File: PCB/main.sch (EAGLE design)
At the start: 55 parts, among them X1 BU-SMA-V

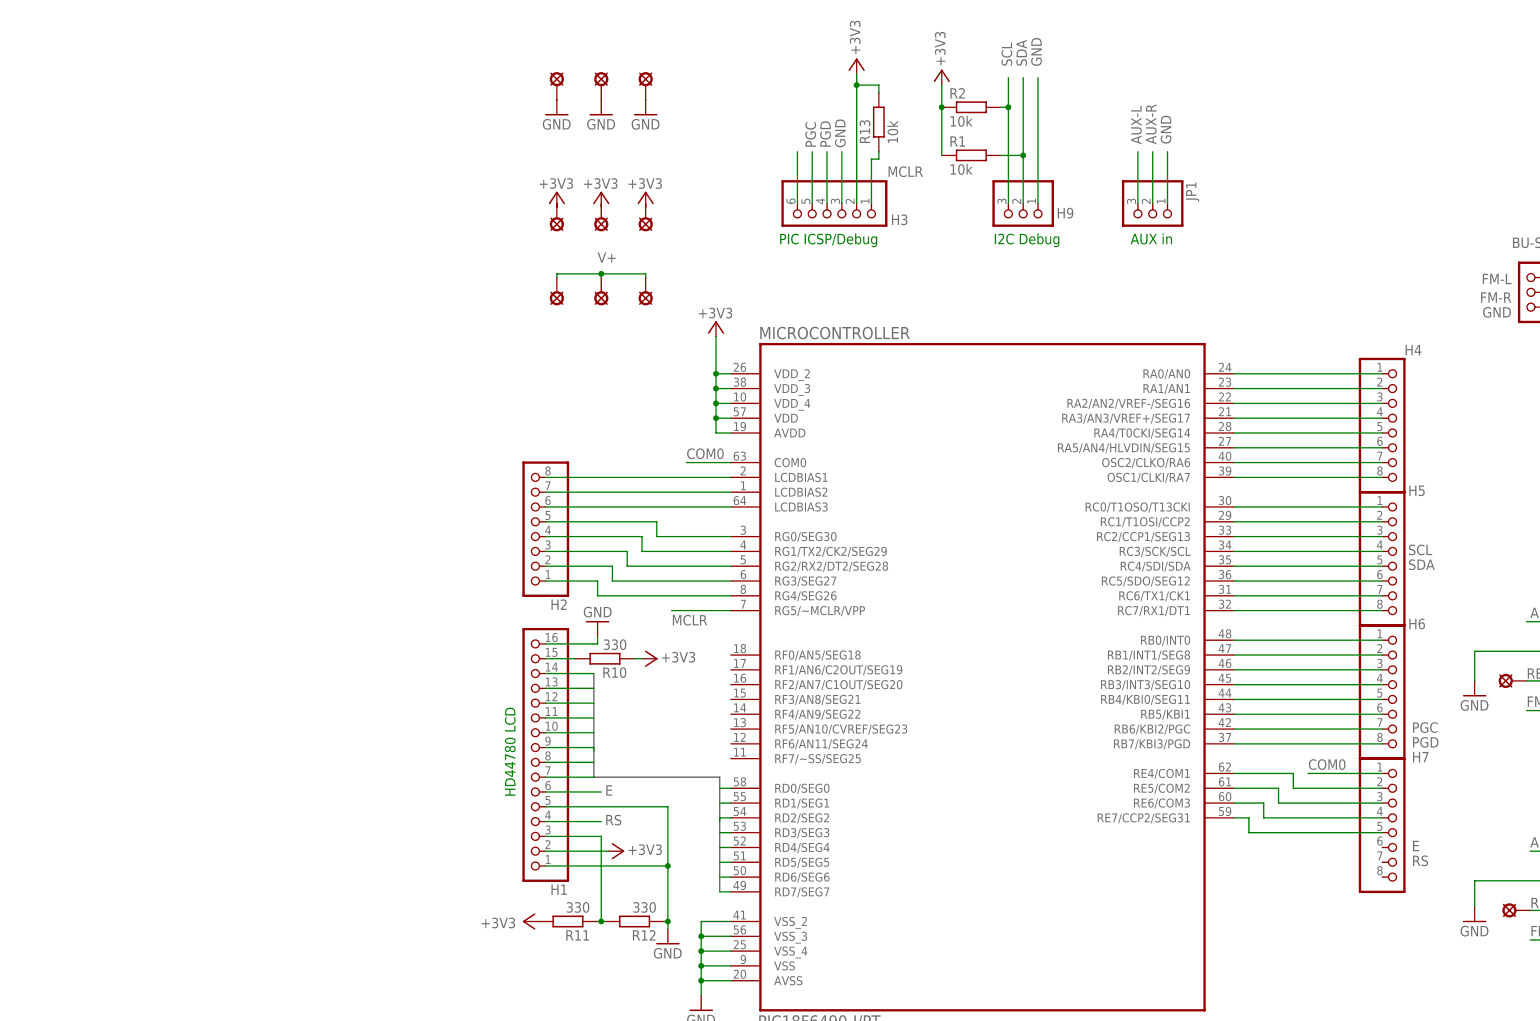
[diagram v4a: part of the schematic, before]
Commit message: Eagle Schematic Changes
- Rearranged PIC pin breakout headers.
- Added REC-in pin header.
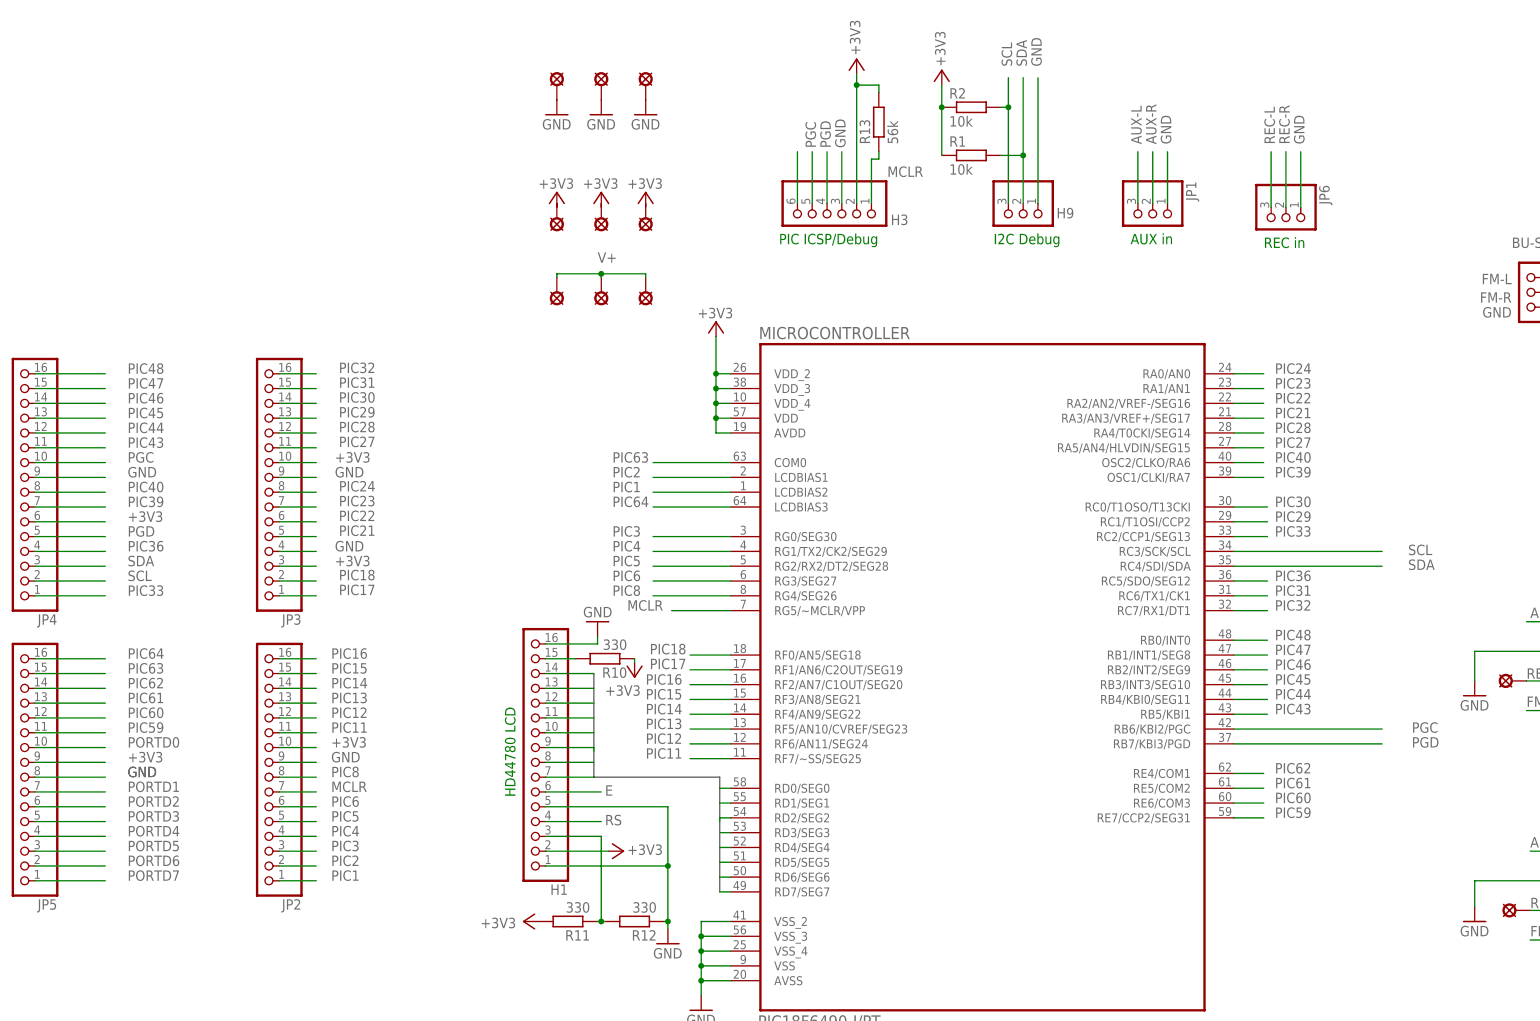
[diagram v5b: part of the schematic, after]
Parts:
- removed H2, H4, H5, H6, H7: (no value), pinhead:PINHD-1X8
- added JP2, JP3, JP4, JP5: (no value), pinhead:PINHD-1X16
- added JP6: (no value), pinhead:PINHD-1X3
- R13: value 10k -> 56k
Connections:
- removed net COM0: H7.1, MICROCONTROLLER.COM0
- removed net N$23: H5.8, MICROCONTROLLER.RC7/RX1/DT1
- removed net N$24: H5.7, MICROCONTROLLER.RC6/TX1/CK1
- removed net N$25: H6.5, MICROCONTROLLER.RB4/KBI0/SEG11
- removed net N$26: H6.4, MICROCONTROLLER.RB3/INT3/SEG10
- removed net N$27: H6.3, MICROCONTROLLER.RB2/INT2/SEG9
- removed net N$28: H6.2, MICROCONTROLLER.RB1/INT1/SEG8
- removed net N$29: H6.1, MICROCONTROLLER.RB0/INT0
- removed net N$30: H5.6, MICROCONTROLLER.RC5/SDO/SEG12
- removed net N$31: H5.3, MICROCONTROLLER.RC2/CCP1/SEG13
- removed net N$32: H5.2, MICROCONTROLLER.RC1/T1OSI/CCP2
- removed net N$33: H5.1, MICROCONTROLLER.RC0/T1OSO/T13CKI
- removed net N$34: H4.8, MICROCONTROLLER.OSC1/CLKI/RA7
- removed net N$35: H4.7, MICROCONTROLLER.OSC2/CLKO/RA6
- removed net N$36: H4.6, MICROCONTROLLER.RA5/AN4/HLVDIN/SEG15
- removed net N$37: H4.5, MICROCONTROLLER.RA4/T0CKI/SEG14
- removed net N$38: H4.4, MICROCONTROLLER.RA3/AN3/VREF+/SEG17
- removed net N$39: H4.3, MICROCONTROLLER.RA2/AN2/VREF-/SEG16
- removed net N$40: H4.2, MICROCONTROLLER.RA1/AN1
- removed net N$41: H4.1, MICROCONTROLLER.RA0/AN0
- removed net N$42: H2.1, MICROCONTROLLER.RG4/SEG26
- removed net N$43: H2.2, MICROCONTROLLER.RG3/SEG27
- removed net N$44: H2.3, MICROCONTROLLER.RG2/RX2/DT2/SEG28
- removed net N$45: H2.4, MICROCONTROLLER.RG1/TX2/CK2/SEG29
- removed net N$46: H2.5, MICROCONTROLLER.RG0/SEG30
- removed net N$47: H2.6, MICROCONTROLLER.LCDBIAS3
- removed net N$48: H2.7, MICROCONTROLLER.LCDBIAS2
- removed net N$49: H2.8, MICROCONTROLLER.LCDBIAS1
- removed net N$50: H7.2, MICROCONTROLLER.RE4/COM1
- removed net N$51: H7.3, MICROCONTROLLER.RE5/COM2
- removed net N$9: H6.6, MICROCONTROLLER.RB5/KBI1
- new net PIC1: JP2.1, MICROCONTROLLER.LCDBIAS2
- new net PIC11: JP2.11, MICROCONTROLLER.RF7/~SS/SEG25
- new net PIC12: JP2.12, MICROCONTROLLER.RF6/AN11/SEG24
- new net PIC13: JP2.13, MICROCONTROLLER.RF5/AN10/CVREF/SEG23
- new net PIC14: JP2.14, MICROCONTROLLER.RF4/AN9/SEG22
- new net PIC15: JP2.15, MICROCONTROLLER.RF3/AN8/SEG21
- new net PIC16: JP2.16, MICROCONTROLLER.RF2/AN7/C1OUT/SEG20
- new net PIC17: JP3.1, MICROCONTROLLER.RF1/AN6/C2OUT/SEG19
- new net PIC18: JP3.2, MICROCONTROLLER.RF0/AN5/SEG18
- new net PIC2: JP2.2, MICROCONTROLLER.LCDBIAS1
- new net PIC21: JP3.5, MICROCONTROLLER.RA3/AN3/VREF+/SEG17
- new net PIC22: JP3.6, MICROCONTROLLER.RA2/AN2/VREF-/SEG16
- new net PIC23: JP3.7, MICROCONTROLLER.RA1/AN1
- new net PIC24: JP3.8, MICROCONTROLLER.RA0/AN0
- new net PIC27: JP3.11, MICROCONTROLLER.RA5/AN4/HLVDIN/SEG15
- new net PIC28: JP3.12, MICROCONTROLLER.RA4/T0CKI/SEG14
- new net PIC29: JP3.13, MICROCONTROLLER.RC1/T1OSI/CCP2
- new net PIC3: JP2.3, MICROCONTROLLER.RG0/SEG30
- new net PIC30: JP3.14, MICROCONTROLLER.RC0/T1OSO/T13CKI
- new net PIC31: JP3.15, MICROCONTROLLER.RC6/TX1/CK1
- new net PIC32: JP3.16, MICROCONTROLLER.RC7/RX1/DT1
- new net PIC33: JP4.1, MICROCONTROLLER.RC2/CCP1/SEG13
- new net PIC36: JP4.4, MICROCONTROLLER.RC5/SDO/SEG12
- new net PIC39: JP4.7, MICROCONTROLLER.OSC1/CLKI/RA7
- new net PIC4: JP2.4, MICROCONTROLLER.RG1/TX2/CK2/SEG29
- new net PIC40: JP4.8, MICROCONTROLLER.OSC2/CLKO/RA6
- new net PIC43: JP4.11, MICROCONTROLLER.RB5/KBI1
- new net PIC44: JP4.12, MICROCONTROLLER.RB4/KBI0/SEG11
- new net PIC45: JP4.13, MICROCONTROLLER.RB3/INT3/SEG10
- new net PIC46: JP4.14, MICROCONTROLLER.RB2/INT2/SEG9
- new net PIC47: JP4.15, MICROCONTROLLER.RB1/INT1/SEG8
- new net PIC48: JP4.16, MICROCONTROLLER.RB0/INT0
- new net PIC5: JP2.5, MICROCONTROLLER.RG2/RX2/DT2/SEG28
- new net PIC59: JP5.11, MICROCONTROLLER.RE7/CCP2/SEG31
- new net PIC6: JP2.6, MICROCONTROLLER.RG3/SEG27
- new net PIC60: JP5.12, MICROCONTROLLER.RE6/COM3
- new net PIC61: JP5.13, MICROCONTROLLER.RE5/COM2
- new net PIC62: JP5.14, MICROCONTROLLER.RE4/COM1
- new net PIC63: JP5.15, MICROCONTROLLER.COM0
- new net PIC64: JP5.16, MICROCONTROLLER.LCDBIAS3
- new net PIC8: JP2.8, MICROCONTROLLER.RG4/SEG26
- net +3V3: now also JP2.10, JP3.10, JP3.3, JP4.6, JP5.9
- net E: no longer H7.4, MICROCONTROLLER.RE6/COM3
- net GND: now also JP2.9, JP3.4, JP3.9, JP4.9, JP5.8, JP6.1
- net MCLR: now also JP2.7
- net PGC: now also JP4.10; no longer H6.7
- net PGD: now also JP4.5; no longer H6.8
- net PORTD0: now also JP5.10
- net PORTD1: now also JP5.7
- net PORTD2: now also JP5.6
- net PORTD3: now also JP5.5
- net PORTD4: now also JP5.4
- net PORTD5: now also JP5.3
- net PORTD6: now also JP5.2
- net PORTD7: now also JP5.1
- net REC-L: now also JP6.3
- net REC-R: now also JP6.2
- net RS: no longer H7.5, MICROCONTROLLER.RE7/CCP2/SEG31
- net SCL: now also JP4.2; no longer H5.4
- net SDA: now also JP4.3; no longer H5.5
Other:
- note added: "REC in"

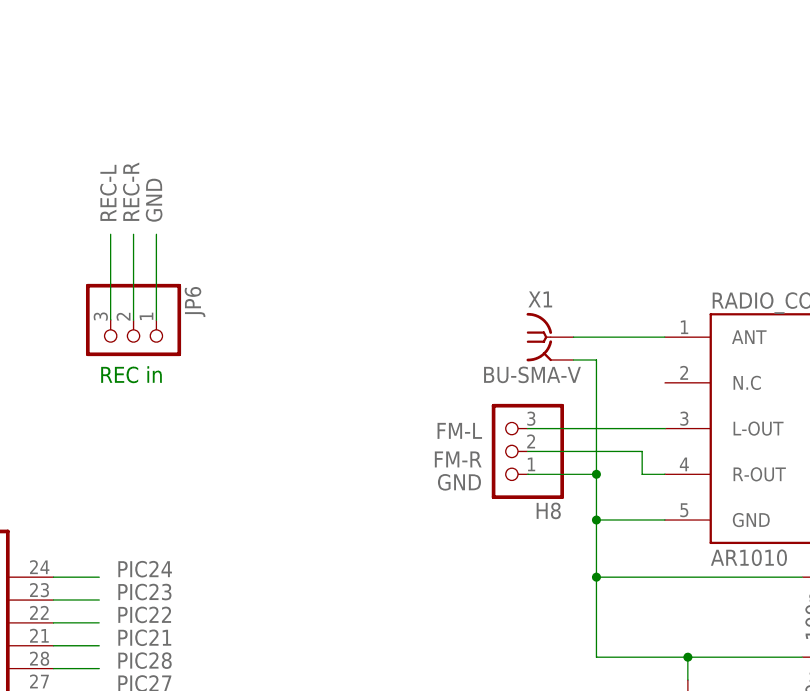
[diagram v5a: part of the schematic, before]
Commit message: Eagle Schematic Changes
- Split off FM out connector
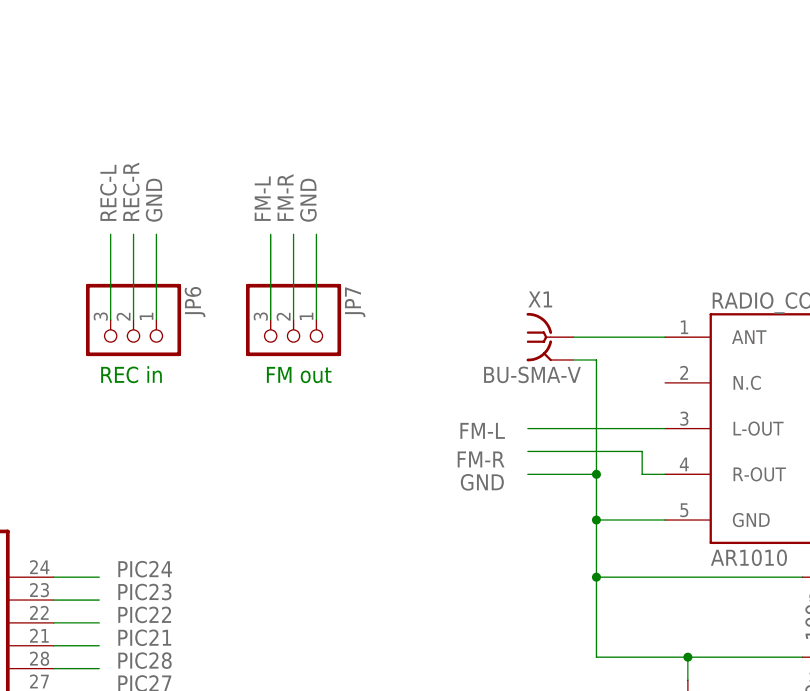
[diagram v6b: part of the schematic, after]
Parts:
- removed H8: (no value), pinhead:PINHD-1X3
- added JP7: (no value), pinhead:PINHD-1X3
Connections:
- net FM-L: now also JP7.3; no longer H8.3
- net FM-R: now also JP7.2; no longer H8.2
- net GND: now also JP7.1; no longer H8.1
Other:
- note added: "FM out"
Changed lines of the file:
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@@
 <part name="R3" library="resistor" deviceset="R-EU_" device="M0805" value="10k"/>
 <part name="H9" library="pinhead" deviceset="PINHD-1X3" device=""/>
-<part name="H8" library="pinhead" deviceset="PINHD-1X3" device=""/>
 <part name="MICROCONTROLLER" library="Microchip_By_element14_Batch_1" deviceset="PIC18F6490-I/PT" device=""/>
 <part name="+3V2" library="supply1" deviceset="+3V3" device=""/>
@@
 <part name="JP5" library="pinhead" deviceset="PINHD-1X16" device=""/>
 <part name="JP6" library="pinhead" deviceset="PINHD-1X3" device=""/>
+<part name="JP7" library="pinhead" deviceset="PINHD-1X3" device=""/>
 </parts>
 <sheets>
@@
 <text x="-22.86" y="49.53" size="1.778" layer="91" rot="R270">HD44780 LCD</text>
 <text x="107.315" y="128.27" size="1.778" layer="91">REC in</text>
+<text x="125.73" y="128.27" size="1.778" layer="91">FM out</text>
 </plain>
 <instances>
@@
 <attribute name="NAME" x="71.755" y="133.35" size="1.778" layer="95"/>
 <attribute name="VALUE" x="58.42" y="139.7" size="1.778" layer="96" rot="R270"/>
-</instance>
-<instance part="H8" gate="A" x="152.4" y="120.65" smashed="yes" rot="R180">
-<attribute name="NAME" x="158.75" y="114.935" size="1.778" layer="95" rot="R180"/>
-<attribute name="VALUE" x="158.75" y="128.27" size="1.778" layer="96" rot="R180"/>
 </instance>
 <instance part="MICROCONTROLLER" gate="A" x="59.055" y="58.42" smashed="yes">
@@
 <instance part="JP5" gate="A" x="-106.045" y="37.465" rot="R180"/>
 <instance part="JP6" gate="A" x="111.125" y="132.715" rot="R270"/>
+<instance part="JP7" gate="A" x="128.905" y="132.715" rot="R270"/>
 </instances>
 <busses>
@@
 <wire x1="185.42" y1="106.68" x2="162.56" y2="106.68" width="0.1524" layer="91"/>
 <junction x="162.56" y="106.68"/>
-<pinref part="H8" gate="A" pin="1"/>
 <wire x1="154.94" y1="118.11" x2="162.56" y2="118.11" width="0.1524" layer="91"/>
 <junction x="162.56" y="118.11"/>
-<label x="149.86" y="118.11" size="1.778" layer="95" rot="R180"/>
+<label x="152.4" y="118.11" size="1.778" layer="95" rot="R180"/>
 <wire x1="172.72" y1="97.79" x2="172.72" y2="95.25" width="0.1524" layer="91"/>
 <junction x="172.72" y="97.79"/>
@@
 <label x="-52.705" y="40.005" size="1.778" layer="95"/>
 </segment>
+<segment>
+<pinref part="JP7" gate="A" pin="1"/>
+<wire x1="131.445" y1="135.255" x2="131.445" y2="144.78" width="0.1524" layer="91"/>
+<label x="131.445" y="146.05" size="1.778" layer="95" rot="R90"/>
+</segment>
 </net>
 <net name="N$4" class="0">
@@
 <wire x1="170.18" y1="118.11" x2="167.64" y2="118.11" width="0.1524" layer="91"/>
 <wire x1="167.64" y1="118.11" x2="167.64" y2="120.65" width="0.1524" layer="91"/>
-<pinref part="H8" gate="A" pin="2"/>
-<label x="149.86" y="120.65" size="1.778" layer="95" rot="R180"/>
+<label x="152.4" y="120.65" size="1.778" layer="95" rot="R180"/>
 <wire x1="167.64" y1="120.65" x2="154.94" y2="120.65" width="0.1524" layer="91"/>
 <pinref part="U$2" gate="G$1" pin="R-OUT"/>
@@
 <pinref part="U$3" gate="G$1" pin="SCL"/>
 </segment>
+<segment>
+<pinref part="JP7" gate="A" pin="2"/>
+<wire x1="128.905" y1="135.255" x2="128.905" y2="144.78" width="0.1524" layer="91"/>
+<label x="128.905" y="146.05" size="1.778" layer="95" rot="R90"/>
+</segment>
 </net>
 <net name="FM-L" class="0">
 <segment>
-<pinref part="H8" gate="A" pin="3"/>
 <wire x1="170.18" y1="123.19" x2="154.94" y2="123.19" width="0.1524" layer="91"/>
-<label x="149.86" y="123.825" size="1.778" layer="95" rot="R180"/>
+<label x="152.4" y="123.825" size="1.778" layer="95" rot="R180"/>
 <pinref part="U$2" gate="G$1" pin="L-OUT"/>
 </segment>
@@
 <pinref part="U$4" gate="G$1" pin="SCL"/>
 </segment>
-</net>
+<segment>
+<pinref part="JP7" gate="A" pin="3"/>
+<wire x1="126.365" y1="135.255" x2="126.365" y2="144.78" width="0.1524" layer="91"/>
+<label x="126.365" y="146.05" size="1.778" layer="95" rot="R90"/>
+</segment>
+</net>

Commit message: Eagle Schematic Changes
Test pins added
Recorder pins added
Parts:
- removed JP1, JP6, JP7: (no value), pinhead:PINHD-1X3
- removed JP3, JP4, JP5: (no value), pinhead:PINHD-1X16
- removed REC-L, REC-R: LSP10, solpad:LSP10
- removed U$4: MAX4586, MAX4586:MAX4586
- added AUX1, H10, H11, H6, H7, H8: (no value), pinhead:PINHD-1X3
- added DISP1, H2: (no value), pinhead:PINHD-1X16
- added H12: (no value), pinhead:PINHD-1X10
- added H5: (no value), pinhead:PINHD-1X6
- added REC1: (no value), pinhead:PINHD-2X5
- added U$1: MAX4586, MAX4586:MAX4586
- H3: device pinhead:PINHD-1X6 -> pinhead:PINHD-1X16
- renumbered JP2 to H4
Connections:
- removed net N$15: C6.1, C7.1, R-OUT.MP
- removed net N$6: C10.1, C9.1, L-OUT.MP
- new net 10: H12.10
- new net 2: H12.2
- new net 3: H12.3
- new net 7: H12.7
- new net 9: H12.9
- new net L-OUT: C10.1, C9.1, H11.3, L-OUT.MP
- new net R-OUT: C6.1, C7.1, H11.2, R-OUT.MP
- net +3V3: now also DISP1.2, H1.9, H2.6, H3.10, H3.3, H5.2, H7.2, U$1.V+, U$3.A, U$3.V+; no longer H1.2, H3.2, JP3.10, JP3.3, JP4.6, JP5.9, U$3.NO2, U$4.NO2, U$4.NO3
- net AMP-L: now also H10.3, U$3.COM; no longer U$4.NO4
- net AMP-R: now also H10.2, U$1.COM; no longer U$3.NO4
- net AUX-L: now also AUX1.3, H9.3, U$3.NO3; no longer JP1.3, U$4.A
- net AUX-R: now also AUX1.2, H9.2, U$1.NO3; no longer JP1.2, U$3.A
- net E: now also DISP1.6; no longer H1.6
- net FM-L: now also H8.3, U$3.NO1; no longer JP7.3, U$4.SCL
- net FM-R: now also H8.2, U$1.NO1; no longer JP7.2, U$3.SCL
- net GND: now also AUX1.1, DISP1.1, DISP1.16, DISP1.5, H1.8, H10.1, H11.1, H2.9, H3.4, H3.9, H5.3, H6.1, H7.1, H8.1, U$1.A, U$1.GND, U$3.GND; no longer H1.1, H1.16, H1.5, H3.3, JP1.1, JP3.4, JP3.9, JP4.9, JP5.8, JP6.1, JP7.1, U$3.NO3, U$3.SDA, U$4.SDA
- net MCLR: now also H5.1; no longer H3.1
- net N$13: now also DISP1.3; no longer H1.3
- net N$18: now also H5.6; no longer H3.6
- net N$2: now also DISP1.15; no longer H1.15
- net PGC: now also H2.10, H5.5; no longer H3.5, JP4.10
- net PGD: now also H2.5, H5.4; no longer H3.4, JP4.5
- net PIC17: now also H3.1; no longer JP3.1
- net PIC18: now also H3.2; no longer JP3.2
- net PIC21: now also H3.5; no longer JP3.5
- net PIC22: now also H3.6; no longer JP3.6
- net PIC23: now also H3.7; no longer JP3.7
- net PIC24: now also H3.8; no longer JP3.8
- net PIC27: now also H3.11; no longer JP3.11
- net PIC28: now also H3.12; no longer JP3.12
- net PIC29: now also H3.13; no longer JP3.13
- net PIC30: now also H3.14; no longer JP3.14
- net PIC31: now also H3.15; no longer JP3.15
- net PIC32: now also H3.16; no longer JP3.16
- net PIC33: now also H2.1; no longer JP4.1
- net PIC36: now also H2.4; no longer JP4.4
- net PIC39: now also H2.7; no longer JP4.7
- net PIC40: now also H2.8; no longer JP4.8
- net PIC43: now also H2.11; no longer JP4.11
- net PIC44: now also H2.12; no longer JP4.12
- net PIC45: now also H2.13; no longer JP4.13
- net PIC46: now also H2.14; no longer JP4.14
- net PIC47: now also H2.15; no longer JP4.15
- net PIC48: now also H2.16; no longer JP4.16
- net PIC59: now also H1.11; no longer JP5.11
- net PIC60: now also H1.12; no longer JP5.12
- net PIC61: now also H1.13; no longer JP5.13
- net PIC62: now also H1.14; no longer JP5.14
- net PIC63: now also H1.15; no longer JP5.15
- net PIC64: now also H1.16; no longer JP5.16
- net PORTD0: now also DISP1.7, H1.10; no longer H1.7, JP5.10
- net PORTD1: now also DISP1.8, H1.7; no longer H1.8, JP5.7
- net PORTD2: now also DISP1.9, H1.6; no longer H1.9, JP5.6
- net PORTD3: now also DISP1.10, H1.5; no longer H1.10, JP5.5
- net PORTD4: now also DISP1.11, H1.4; no longer H1.11, JP5.4
- net PORTD5: now also DISP1.12, H1.3; no longer H1.12, JP5.3
- net PORTD6: now also DISP1.13, H1.2; no longer H1.13, JP5.2
- net PORTD7: now also DISP1.14, H1.1; no longer H1.14, JP5.1
- net REC-L: now also U$3.NO2; no longer JP6.3, REC-L.MP, U$4.V+
- net REC-R: now also U$1.NO2; no longer JP6.2, REC-R.MP, U$3.V+
- net RS: now also DISP1.4; no longer H1.4
- net SCL: now also H2.2, H6.3, U$1.SCL, U$3.SCL; no longer H9.3, JP4.2, U$3.NO1, U$4.NO1
- net SDA: now also H2.3, H6.2, U$1.SDA, U$3.SDA; no longer H9.2, JP4.3, U$3.GND, U$4.GND
- net V+: now also H12.1, H12.6, H7.3, REC1.1
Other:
- note added: "AMP test"
- note added: "AUX test"
- note added: "Output test"
- note added: "Radio test"
- note added: "Recorder test"
- note added: "Voltage test"
- note removed: "AUX in"
- note removed: "FM out"
- note removed: "REC in"
- moved on the sheet: H1, H9, R1, R10, R11, R12, R13, R2
